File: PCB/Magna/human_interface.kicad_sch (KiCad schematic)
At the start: 0 parts

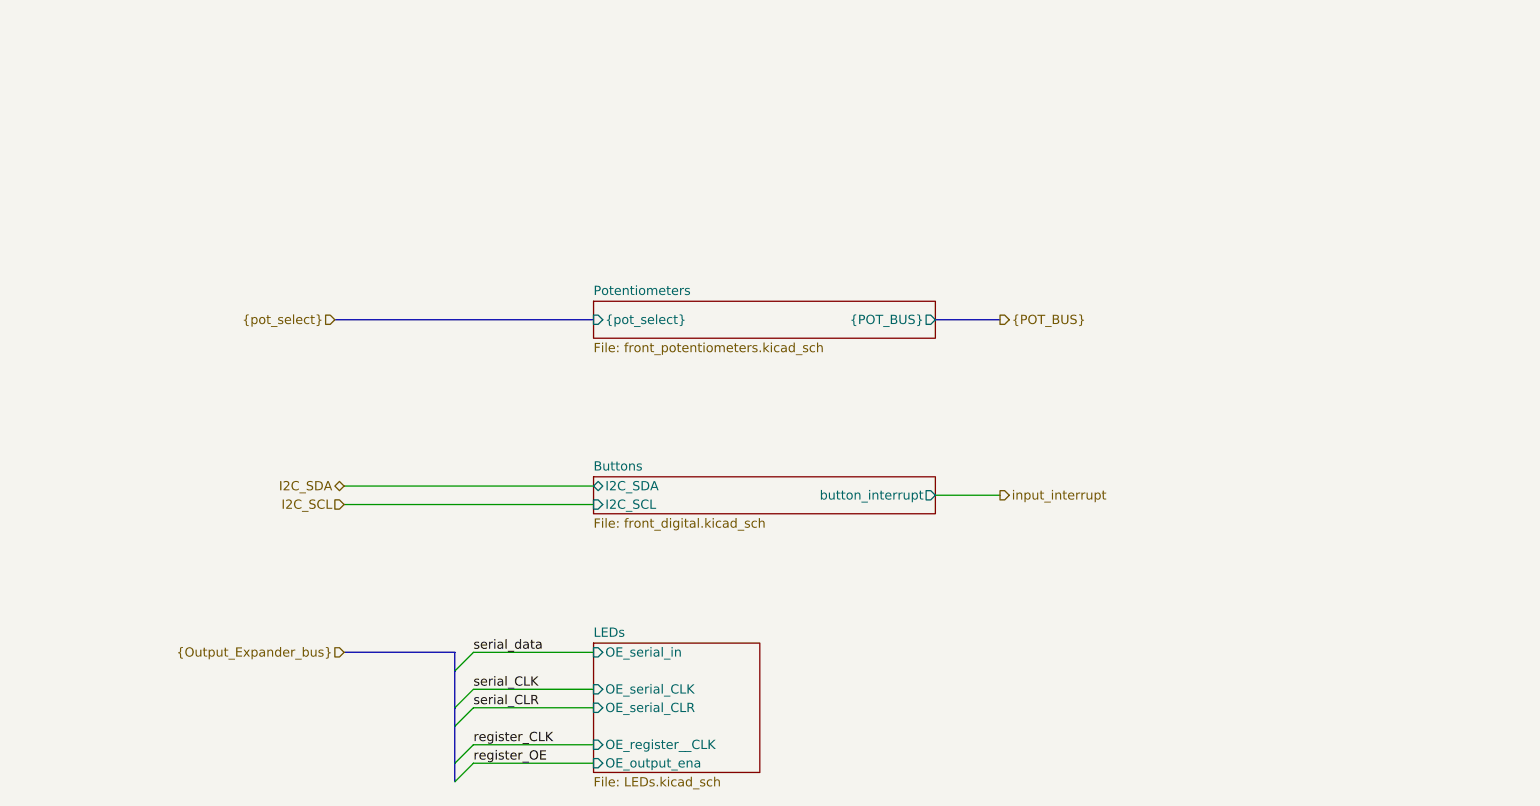
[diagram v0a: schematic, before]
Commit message: Split schematic to several projects
To allow for several boards to be done a kicad project
is needed for each
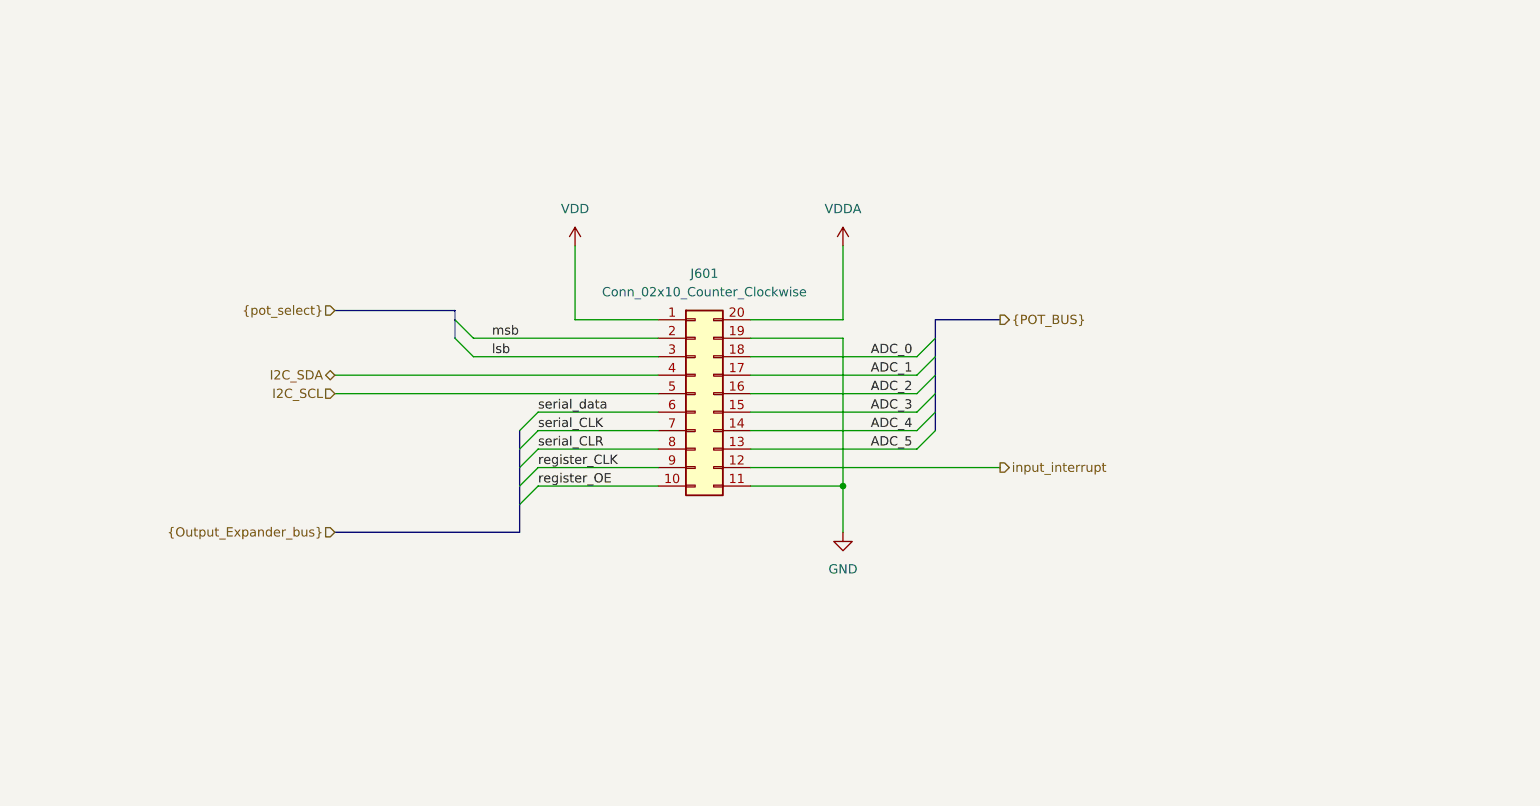
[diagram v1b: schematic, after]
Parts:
- added J601: Conn_02x10_Counter_Clockwise, Connector_PinSocket_2.54mm:PinSocket_2x10_P2.54mm_Vertical, symbol Connector_Generic:Conn_02x10_Counter_Clockwise
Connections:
- net I2C_SCL: now also J601.5 (Pin_5)
- net I2C_SDA: now also J601.4 (Pin_4)
- net input_interrupt: now also J601.12 (Pin_12)
- net register_CLK: now also J601.9 (Pin_9)
- net register_OE: now also J601.10 (Pin_10)
- net serial_CLK: now also J601.7 (Pin_7)
- net serial_CLR: now also J601.8 (Pin_8)
- net serial_data: now also J601.6 (Pin_6)
- new net ADC_0: J601.18 (Pin_18)
- new net ADC_1: J601.17 (Pin_17)
- new net ADC_2: J601.16 (Pin_16)
- new net ADC_3: J601.15 (Pin_15)
- new net ADC_4: J601.14 (Pin_14)
- new net ADC_5: J601.13 (Pin_13)
- new net GND: J601.11 (Pin_11), J601.19 (Pin_19)
- new net VDD: J601.1 (Pin_1)
- new net VDDA: J601.20 (Pin_20)
- new net lsb: J601.3 (Pin_3)
- new net msb: J601.2 (Pin_2)
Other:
- removed sheet Buttons
- removed sheet LEDs
- removed sheet Potentiometers

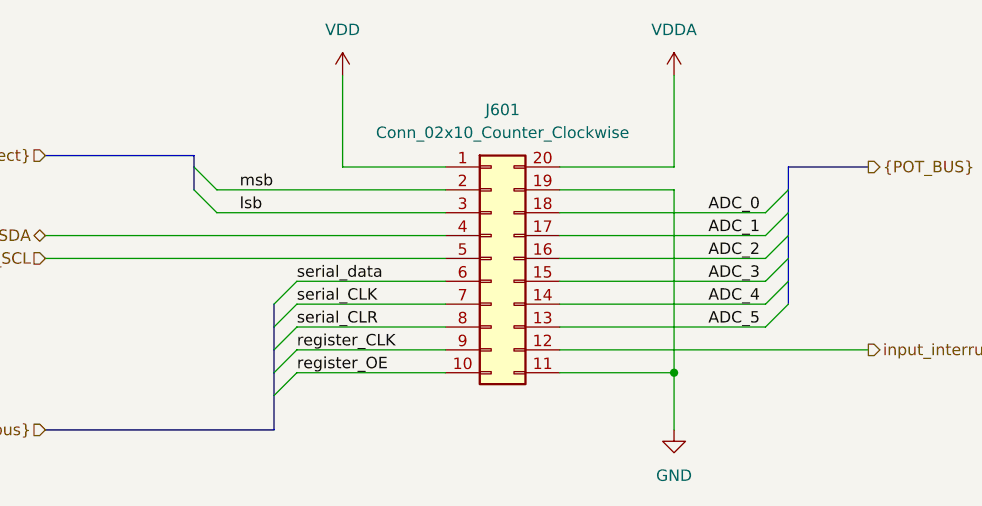
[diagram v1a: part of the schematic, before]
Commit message: Change connector to IO board
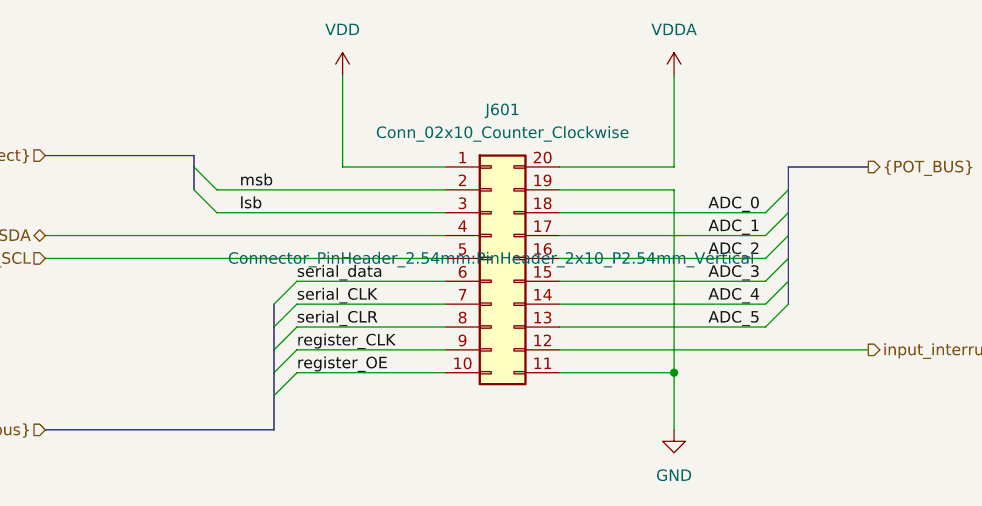
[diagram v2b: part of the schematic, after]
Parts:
- J601: footprint Connector_PinSocket_2.54mm:PinSocket_2x10_P2.54mm_Vertical -> Connector_PinHeader_2.54mm:PinHeader_2x10_P2.54mm_Vertical
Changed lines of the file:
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@@
     (effects (font (size 1.27 1.27)) (justify left bottom))
   )
-  (label "ADC_0" (at 162.56 67.31 0)
+  (label "ADC_0" (at 162.56 67.31 0) (fields_autoplaced)
     (effects (font (size 1.27 1.27)) (justify left bottom))
   )
@@
     (effects (font (size 1.27 1.27)) (justify left bottom))
   )
-  (label "msb" (at 110.49 64.77 0)
+  (label "msb" (at 110.49 64.77 0) (fields_autoplaced)
     (effects (font (size 1.27 1.27)) (justify left bottom))
   )
-  (label "lsb" (at 110.49 67.31 0)
+  (label "lsb" (at 110.49 67.31 0) (fields_autoplaced)
     (effects (font (size 1.27 1.27)) (justify left bottom))
   )
@@
       (effects (font (size 1.27 1.27)))
     )
-    (property "Footprint" "Connector_PinSocket_2.54mm:PinSocket_2x10_P2.54mm_Vertical" (at 138.43 72.39 0)
-      (effects (font (size 1.27 1.27)) hide)
+    (property "Footprint" "Connector_PinHeader_2.54mm:PinHeader_2x10_P2.54mm_Vertical" (at 138.43 72.39 0)
+      (effects (font (size 1.27 1.27)))
     )
     (property "Datasheet" "~" (at 138.43 72.39 0)

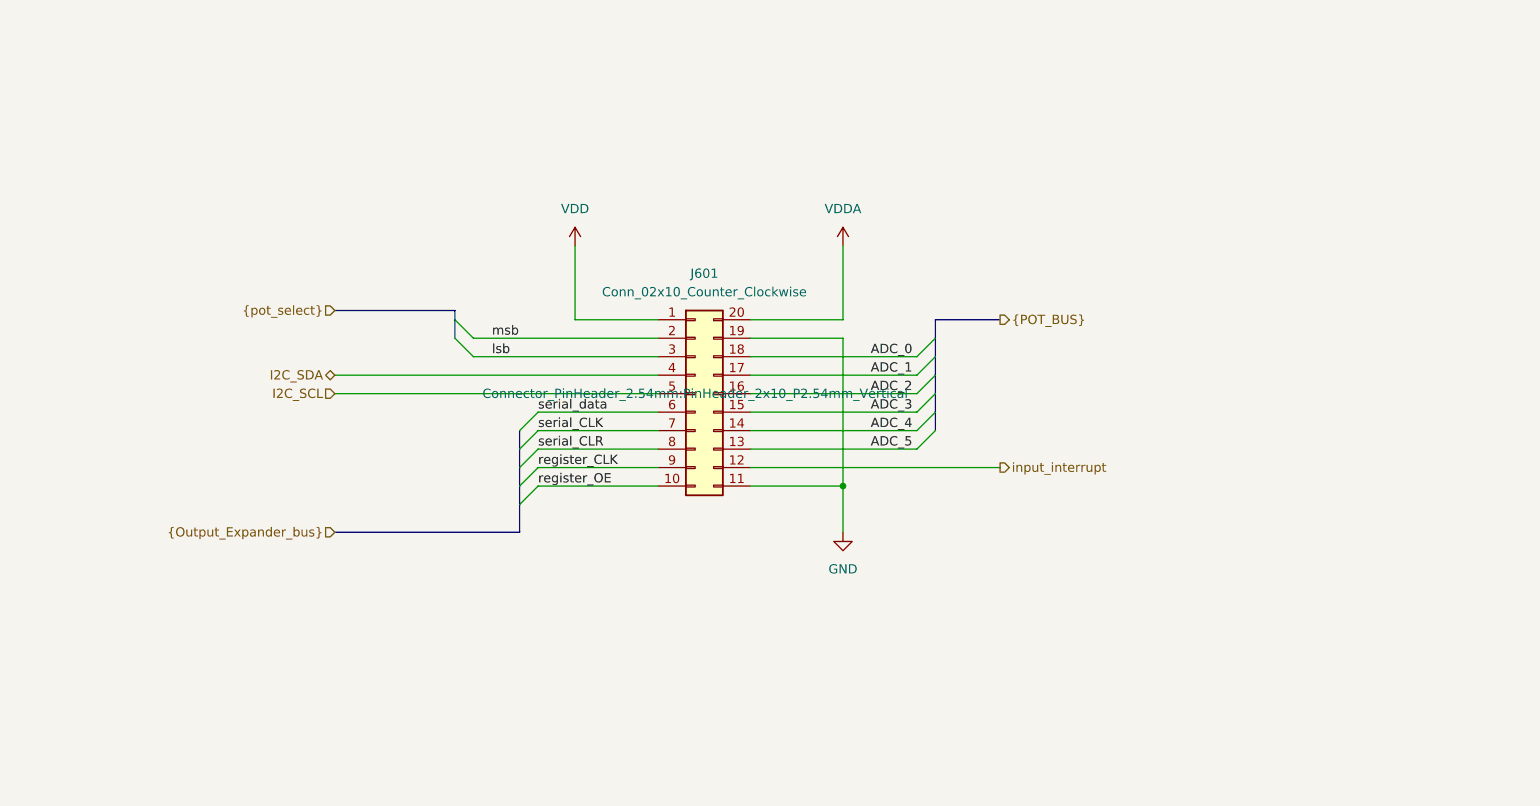
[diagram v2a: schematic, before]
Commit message: Mainboard layout (#19)
Also adds mounting holes to IO daughterboard
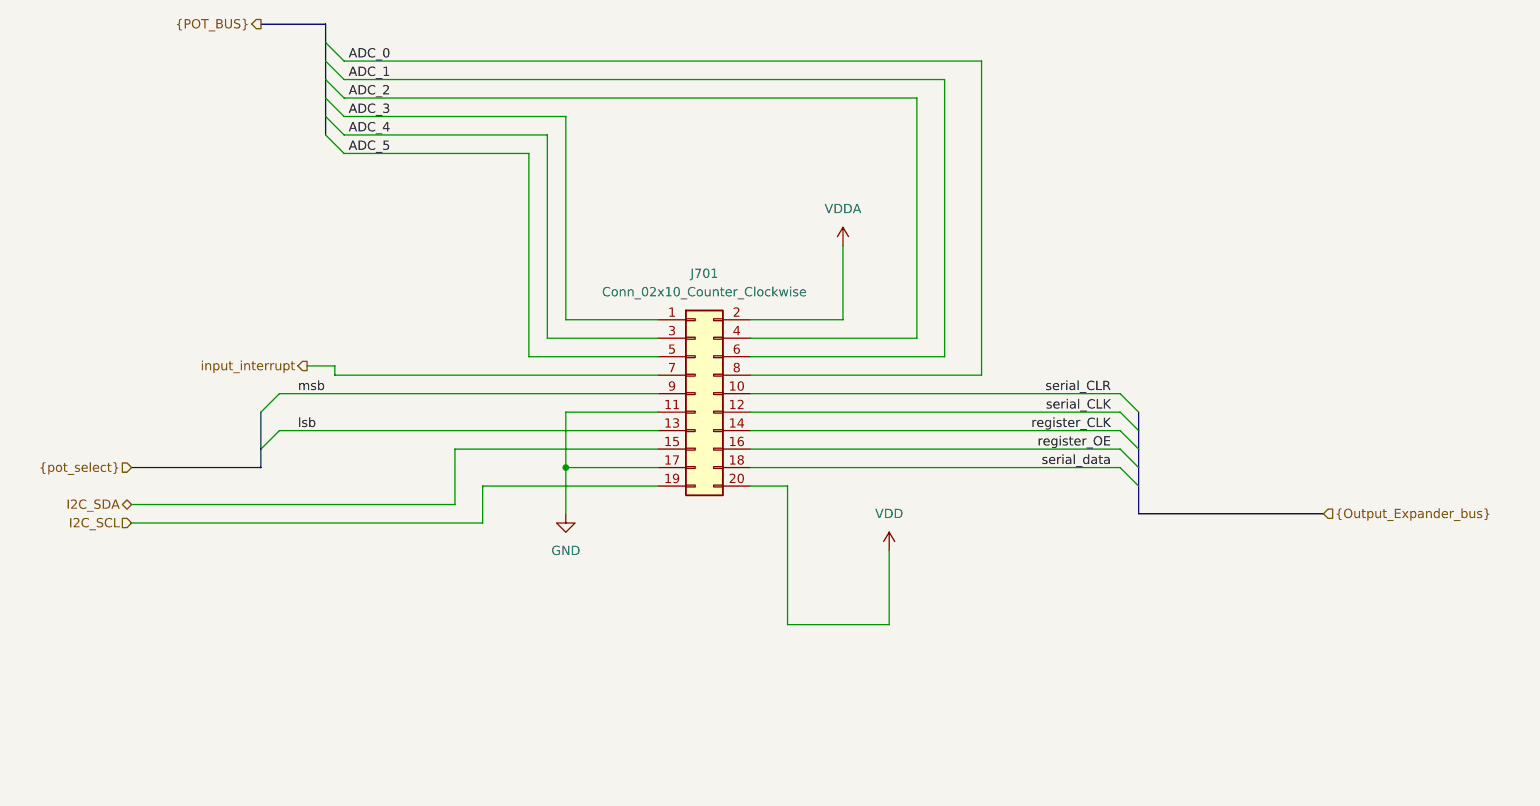
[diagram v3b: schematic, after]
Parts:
- J701: renamed from J601; footprint Connector_PinHeader_2.54mm:PinHeader_2x10_P2.54mm_Vertical -> Connector_PinHeader_2.54mm:PinHeader_2x10_P2.54mm_Horizontal; symbol Connector_Generic:Conn_02x10_Counter_Clockwise -> Connector_Generic:Conn_02x10_Odd_Even
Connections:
- net ADC_0: now also J701.8 (Pin_8); no longer J701.18 (Pin_18)
- net ADC_1: now also J701.6 (Pin_6); no longer J701.17 (Pin_17)
- net ADC_2: now also J701.4 (Pin_4); no longer J701.16 (Pin_16)
- net ADC_3: now also J701.1 (Pin_1); no longer J701.15 (Pin_15)
- net ADC_4: now also J701.3 (Pin_3); no longer J701.14 (Pin_14)
- net ADC_5: now also J701.5 (Pin_5); no longer J701.13 (Pin_13)
- net GND: now also J701.17 (Pin_17); no longer J701.19 (Pin_19)
- net I2C_SCL: now also J701.19 (Pin_19); no longer J701.5 (Pin_5)
- net I2C_SDA: now also J701.15 (Pin_15); no longer J701.4 (Pin_4)
- net VDD: now also J701.20 (Pin_20); no longer J701.1 (Pin_1)
- net VDDA: now also J701.2 (Pin_2); no longer J701.20 (Pin_20)
- net input_interrupt: now also J701.7 (Pin_7); no longer J701.12 (Pin_12)
- net lsb: now also J701.13 (Pin_13); no longer J701.3 (Pin_3)
- net msb: now also J701.9 (Pin_9); no longer J701.2 (Pin_2)
- net register_CLK: now also J701.14 (Pin_14); no longer J701.9 (Pin_9)
- net register_OE: now also J701.16 (Pin_16); no longer J701.10 (Pin_10)
- net serial_CLK: now also J701.12 (Pin_12); no longer J701.7 (Pin_7)
- net serial_CLR: now also J701.10 (Pin_10); no longer J701.8 (Pin_8)
- net serial_data: now also J701.18 (Pin_18); no longer J701.6 (Pin_6)

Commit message: Some updates to PCB
Honestly I cannot remember whats changed
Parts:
- J701: now left out of the parts list
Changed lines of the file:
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@@
 		(unit 1)
 		(exclude_from_sim no)
-		(in_bom yes)
+		(in_bom no)
 		(on_board yes)
 		(dnp no)
